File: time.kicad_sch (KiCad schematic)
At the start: 10 parts, among them Y1 32.768k

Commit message: WIP
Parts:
- added J7, J8, J9: Conn_01x04_Socket, Connector_PinHeader_2.54mm:PinHeader_1x04_P2.54mm_Vertical, symbol Connector:Conn_01x04_Socket
- C10, C11, C9: footprint (none) -> Capacitor_SMD:C_0603_1608Metric_Pad1.08x0.95mm_HandSolder
- C12: footprint (none) -> Capacitor_SMD:C_0603_1608Metric_Pad1.08x0.95mm_HandSolder; Manufacturer Product Number (none) -> FME0H473ZF
- R26: renamed from R25; footprint (none) -> Resistor_SMD:R_0603_1608Metric_Pad0.98x0.95mm_HandSolder
- R27: renamed from R26; footprint (none) -> Resistor_SMD:R_0603_1608Metric_Pad0.98x0.95mm_HandSolder
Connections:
- net ALARM: now also J9.2 (Pin_2)
- net GND: now also J8.3 (Pin_3), J8.4 (Pin_4)
- net SPI0.MISO: now also J7.2 (Pin_2)
- net SPI0.MOSI: now also J7.3 (Pin_3)
- net SPI0.SCK: now also J7.1 (Pin_1)
- net SPI0.~{CS3}: now also J7.4 (Pin_4)
- net V_{3.3}: now also J8.2 (Pin_2)
- net V_{ADP}: now also J8.1 (Pin_1)
- net V_{RTC}: now also J9.1 (Pin_1)
- no-connect marks 3 -> 5
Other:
- note added: "ESR 20 ohm at 1kHz"
- note added: "This diode allows trickle charging the RTC backup capacitor when ( V_{ADP} - 0.3 ) < V_{C}"
- moved on the sheet: D1, D2

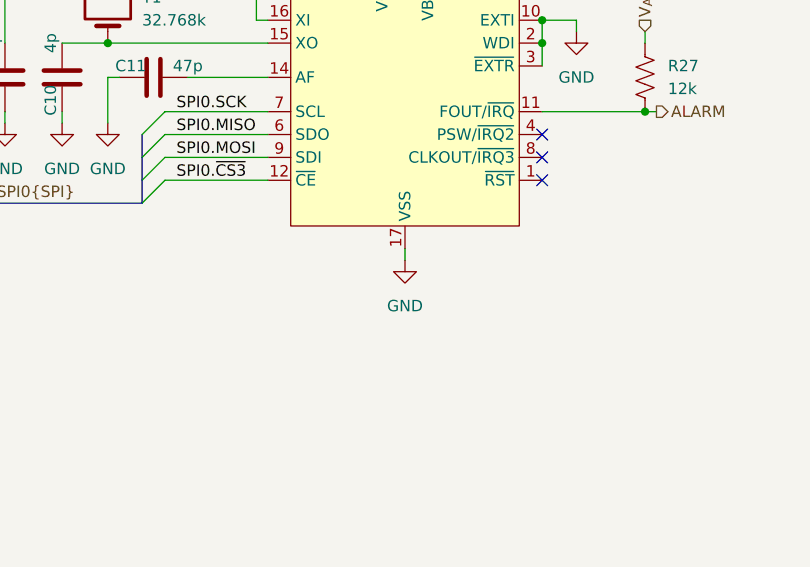
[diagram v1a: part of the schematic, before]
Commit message: Layout cleanups, add more component data
 - Selected part for USB C socket
 - Tried to make more of the schematics compact and modular
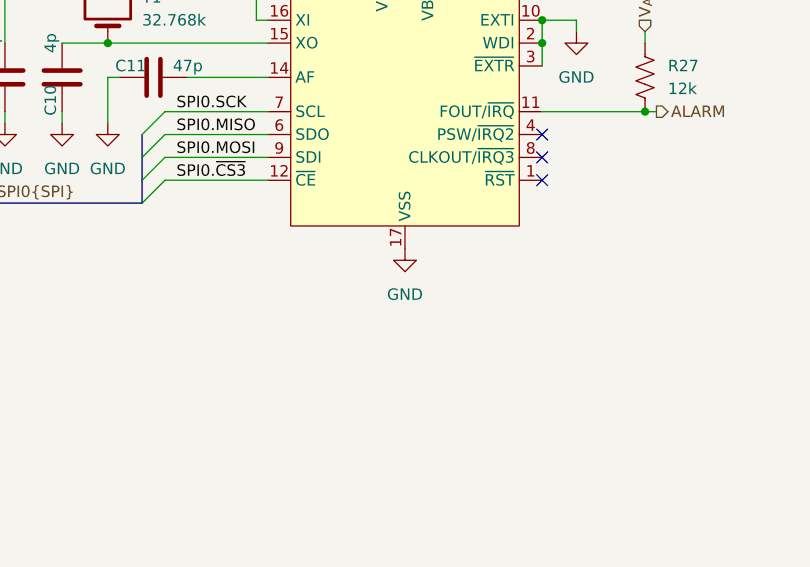
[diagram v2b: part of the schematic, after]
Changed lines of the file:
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@@
-    (stroke (width 0) (type default))
-  )
-  (wire (pts (xy 135.89 111.76) (xy 135.89 113.03))
     (stroke (width 0) (type default))
   )
@@
     )
   )
-  (symbol (lib_id "power:GND") (at 135.89 113.03 0) (unit 1)
-    (in_bom yes) (on_board yes) (dnp no) (fields_autoplaced)
-    (property "Reference" "#PWR038" (at 135.89 119.38 0)
-      (effects (font (size 1.27 1.27)) hide)
-    )
-    (property "Value" "GND" (at 135.89 118.11 0)
-      (effects (font (size 1.27 1.27)))
-    )
-    (property "Footprint" "" (at 135.89 113.03 0)
-      (effects (font (size 1.27 1.27)) hide)
-    )
-    (property "Datasheet" "" (at 135.89 113.03 0)
-      (effects (font (size 1.27 1.27)) hide)
-    )
+  (symbol (lib_id "power:GND") (at 135.89 111.76 0) (unit 1)
+    (in_bom yes) (on_board yes) (dnp no) (fields_autoplaced)
+    (property "Reference" "#PWR038" (at 135.89 118.11 0)
+      (effects (font (size 1.27 1.27)) hide)
+    )
+    (property "Value" "GND" (at 135.89 116.84 0)
+      (effects (font (size 1.27 1.27)))
+    )
+    (property "Footprint" "" (at 135.89 111.76 0)
+      (effects (font (size 1.27 1.27)) hide)
+    )
+    (property "Datasheet" "" (at 135.89 111.76 0)
+      (effects (font (size 1.27 1.27)) hide)
+    )

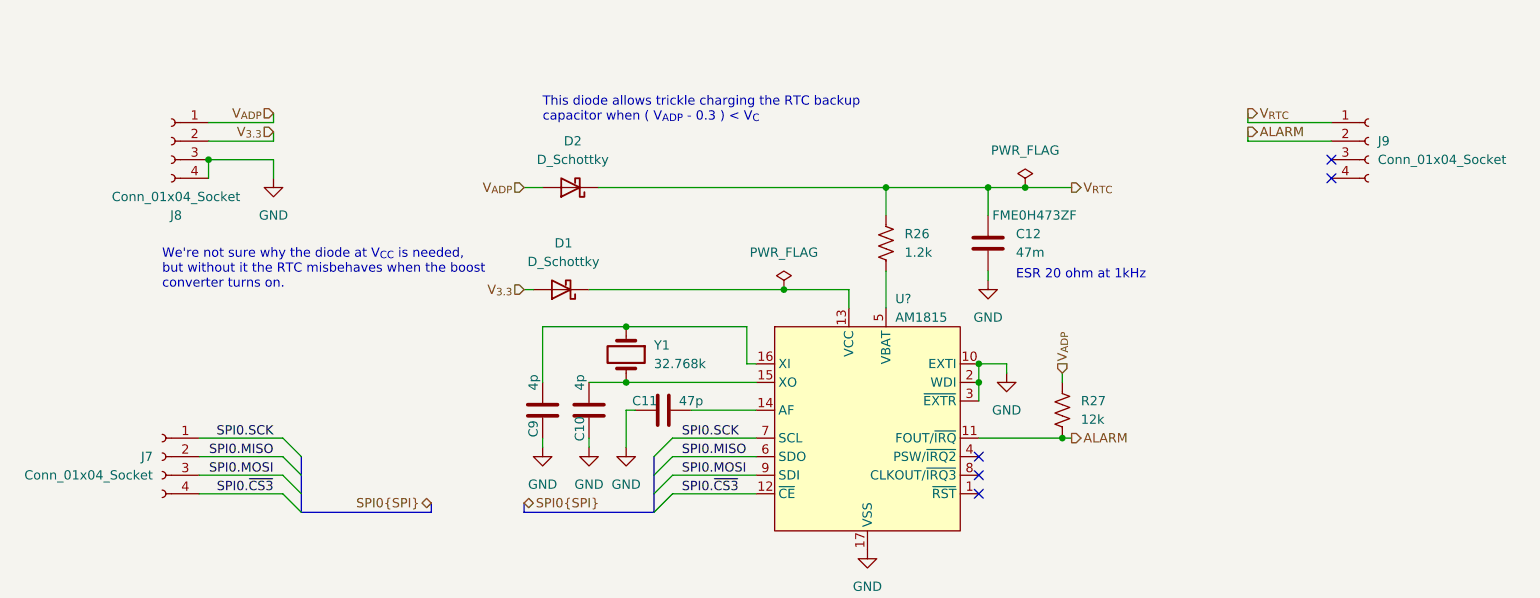
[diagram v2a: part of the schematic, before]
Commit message: First routing attempt
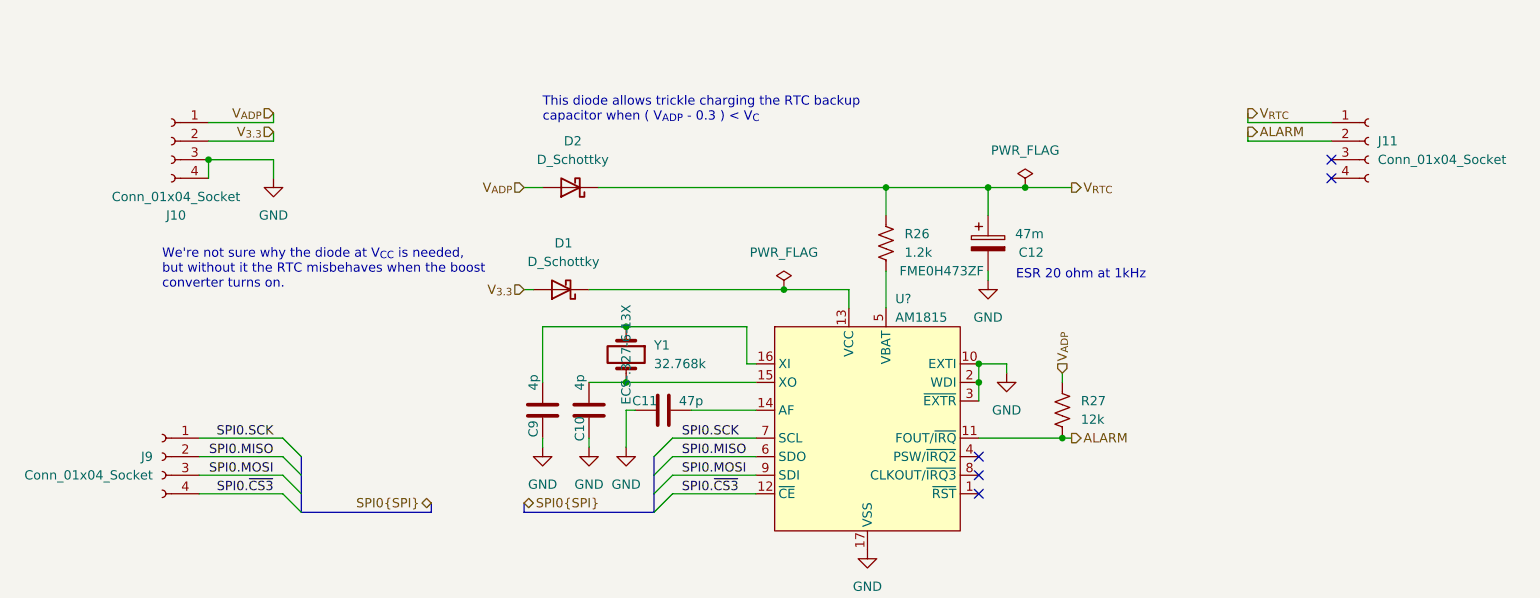
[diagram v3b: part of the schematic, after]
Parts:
- C12: footprint Capacitor_SMD:C_0603_1608Metric_Pad1.08x0.95mm_HandSolder -> Capacitor_THT:CP_Radial_D4.0mm_P1.50mm; symbol Device:C -> Device:C_Polarized
- D1, D2: footprint (none) -> Diode_SMD:D_SOD-323; Digikey Product Number (none) -> 3757-RB751V-40_R1_00001CT-ND; Manufacturer Product Number (none) -> RB751V-40_R1_00001
- U?: footprint (none) -> Package_DFN_QFN:VQFN-16-1EP_3x3mm_P0.5mm_EP1.8x1.8mm; Digikey Product Number (none) -> 5128-AM1815AQCT-ND; Manufacturer Product Number (none) -> AM1815AQ
- Y1: footprint (none) -> Crystal:Crystal_DS26_D2.0mm_L6.0mm_Vertical; Digikey Product Number (none) -> XC2293-ND; Manufacturer Product Number (none) -> ECS-.327-6-13X
- renumbered J8 to J10, J9 to J11, J7 to J9
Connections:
- net GND: now also C12.2; no longer C12.1
- net V_{RTC}: now also C12.1; no longer C12.2
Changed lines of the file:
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@@
       (effects (font (size 1.27 1.27)))
     )
-    (property "Footprint" "" (at 95.25 62.23 0)
-      (effects (font (size 1.27 1.27)) hide)
-    )
-    (property "Datasheet" "~" (at 95.25 62.23 0)
+    (property "Footprint" "Diode_SMD:D_SOD-323" (at 95.25 62.23 0)
+      (effects (font (size 1.27 1.27)) hide)
+    )
+    (property "Datasheet" "https://www.panjit.com.tw/upload/datasheet/RB751V-40.pdf" (at 95.25 62.23 0)
+      (effects (font (size 1.27 1.27)) hide)
+    )
+    (property "Digikey Product Number" "3757-RB751V-40_R1_00001CT-ND" (at 95.25 62.23 0)
+      (effects (font (size 1.27 1.27)) hide)
+    )
+    (property "Manufacturer Product Number" "RB751V-40_R1_00001" (at 95.25 62.23 0)
       (effects (font (size 1.27 1.27)) hide)
     )
@@
   (symbol (lib_id "Connector:Conn_01x04_Socket") (at 39.37 99.06 0) (mirror y) (unit 1)
     (in_bom yes) (on_board yes) (dnp no)
-    (property "Reference" "J7" (at 38.1 99.06 0)
+    (property "Reference" "J9" (at 38.1 99.06 0)
       (effects (font (size 1.27 1.27)) (justify left))
     )
@@
       (project "artemia"
         (path "/3ef271cf-72c1-43e9-bc06-d7d78e288e38/9bab1f2e-658f-484a-8e5a-6de6f47dc750"
-          (reference "J7") (unit 1)
+          (reference "J9") (unit 1)
         )
       )
@@
       (effects (font (size 1.27 1.27)) (justify left))
     )
-    (property "Footprint" "" (at 102.87 85.09 0)
-      (effects (font (size 1.27 1.27)) hide)
-    )
-    (property "Datasheet" "~" (at 102.87 85.09 0)
+    (property "Footprint" "Crystal:Crystal_DS26_D2.0mm_L6.0mm_Vertical" (at 102.87 85.09 0)
+      (effects (font (size 1.27 1.27)) hide)
+    )
+    (property "Datasheet" "https://ecsxtal.com/store/pdf/ECS-3x8X%202x6X%201X5X.pdf" (at 102.87 85.09 0)
+      (effects (font (size 1.27 1.27)) hide)
+    )
+    (property "Manufacturer Product Number" "ECS-.327-6-13X" (at 102.87 85.09 0)
+      (effects (font (size 1.27 1.27)))
+    )
+    (property "Digikey Product Number" "XC2293-ND" (at 102.87 85.09 0)
+      (effects (font (size 1.27 1.27)) hide)
+    )
+    (property "Mouser Product Number" "" (at 102.87 85.09 0)
       (effects (font (size 1.27 1.27)) hide)
     )
@@
     )
   )
-  (symbol (lib_id "Device:C") (at 152.4 69.85 180) (unit 1)
-    (in_bom yes) (on_board yes) (dnp no)
-    (property "Reference" "C12" (at 156.21 68.58 0)
+  (symbol (lib_id "Device:C_Polarized") (at 152.4 69.85 0) (unit 1)
+    (in_bom yes) (on_board yes) (dnp no)
+    (property "Reference" "C12" (at 160.02 71.12 0)
       (effects (font (size 1.27 1.27)) (justify right))
     )
-    (property "Value" "47m" (at 156.21 71.12 0)
+    (property "Value" "47m" (at 160.02 68.58 0)
       (effects (font (size 1.27 1.27)) (justify right))
     )
-    (property "Footprint" "Capacitor_SMD:C_0603_1608Metric_Pad1.08x0.95mm_HandSolder" (at 151.4348 66.04 0)
-      (effects (font (size 1.27 1.27)) hide)
-    )
-    (property "Datasheet" "https://connect.kemet.com:7667/gateway/IntelliData-ComponentDocumentation/1.0/download/datasheet/FMC0H334ZF" (at 152.4 69.85 0)
-      (effects (font (size 1.27 1.27)) hide)
-    )
-    (property "Manufacturer Product Number" "FME0H473ZF" (at 158.75 66.04 0)
-      (effects (font (size 1.27 1.27)))
+    (property "Footprint" "Capacitor_THT:CP_Radial_D4.0mm_P1.50mm" (at 153.3652 73.66 0)
+      (effects (font (size 1.27 1.27)) hide)
+    )
+    (property "Datasheet" "~" (at 152.4 69.85 0)
+      (effects (font (size 1.27 1.27)) hide)
+    )
+    (property "Manufacturer Product Number" "FME0H473ZF" (at 146.05 73.66 0)
+      (effects (font (size 1.27 1.27)))
+    )
+    (property "Digikey Product Number" "" (at 152.4 69.85 0)
+      (effects (font (size 1.27 1.27)) hide)
+    )
+    (property "Mouser Product Number" "" (at 152.4 69.85 0)
+      (effects (font (size 1.27 1.27)) hide)
     )
     (pin "1")
@@
   (symbol (lib_id "Connector:Conn_01x04_Socket") (at 40.64 55.88 0) (mirror y) (unit 1)
     (in_bom yes) (on_board yes) (dnp no)
-    (property "Reference" "J8" (at 41.275 66.04 0)
+    (property "Reference" "J10" (at 41.275 66.04 0)
       (effects (font (size 1.27 1.27)))
     )
@@
       (project "artemia"
         (path "/3ef271cf-72c1-43e9-bc06-d7d78e288e38/9bab1f2e-658f-484a-8e5a-6de6f47dc750"
-          (reference "J8") (unit 1)
+          (reference "J10") (unit 1)
         )
       )
@@
       (effects (font (size 1.27 1.27)))
     )
-    (property "Footprint" "" (at 93.98 76.2 0)
-      (effects (font (size 1.27 1.27)) hide)
-    )
-    (property "Datasheet" "~" (at 93.98 76.2 0)
+    (property "Footprint" "Diode_SMD:D_SOD-323" (at 93.98 76.2 0)
+      (effects (font (size 1.27 1.27)) hide)
+    )
+    (property "Datasheet" "https://www.panjit.com.tw/upload/datasheet/RB751V-40.pdf" (at 93.98 76.2 0)
+      (effects (font (size 1.27 1.27)) hide)
+    )
+    (property "Digikey Product Number" "3757-RB751V-40_R1_00001CT-ND" (at 93.98 76.2 0)
+      (effects (font (size 1.27 1.27)) hide)
+    )
+    (property "Manufacturer Product Number" "RB751V-40_R1_00001" (at 93.98 76.2 0)
       (effects (font (size 1.27 1.27)) hide)
     )
@@
       (effects (font (size 1.27 1.27)) (justify left))
     )
-    (property "Footprint" "" (at 135.89 91.44 0)
+    (property "Footprint" "Package_DFN_QFN:VQFN-16-1EP_3x3mm_P0.5mm_EP1.8x1.8mm" (at 135.89 91.44 0)
       (effects (font (size 1.27 1.27)) hide)
     )
     (property "Datasheet" "https://ambiq.com/artasie-am1815/" (at 135.89 91.44 0)
+      (effects (font (size 1.27 1.27)) hide)
+    )
+    (property "Digikey Product Number" "5128-AM1815AQCT-ND" (at 135.89 93.98 0)
+      (effects (font (size 1.27 1.27)) hide)
+    )
+    (property "Manufacturer Product Number" "AM1815AQ" (at 135.89 93.98 0)
       (effects (font (size 1.27 1.27)) hide)
     )
@@
   (symbol (lib_id "Connector:Conn_01x04_Socket") (at 204.47 55.88 0) (unit 1)
     (in_bom yes) (on_board yes) (dnp no) (fields_autoplaced)
-    (property "Reference" "J9" (at 205.74 55.88 0)
+    (property "Reference" "J11" (at 205.74 55.88 0)
       (effects (font (size 1.27 1.27)) (justify left))
     )
@@
       (project "artemia"
         (path "/3ef271cf-72c1-43e9-bc06-d7d78e288e38/9bab1f2e-658f-484a-8e5a-6de6f47dc750"
-          (reference "J9") (unit 1)
-        )
-      )
+          (reference "J11") (unit 1)
+        )
+      )
